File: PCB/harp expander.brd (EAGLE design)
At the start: 124.5 x 80.4 mm, 132 parts, among them IC1 XMEGA-A1TQFP, IC14 SN74LVC1G125DBVT, IC2 USBLC6-2SC6, IC3 FT232RL, IC4 TLV70033DDCR, IC5 TLV70033DDCR, IC6 SI8610BC-B-IS, IC7 SN74LVC1G125DBVT, T10 BC850, T11 BC850, T12 BC850, T13 BC850, T2 BC850, T3 BC850, T4 BC850, T5 BC850, T6 BC850, T7 BC850, T8 BC850, T9 BC850, U1 744245X, U2 744245X

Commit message: Minor corrections.
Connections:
- net IO_BUTTON0 renamed AUX_IN0
- net IO_BUTTON1 renamed AUX_IN1
- net PD0 renamed IO4_UC
- net PD1 renamed IO3_UC
- net PD2 renamed IO2_UC
- net PD3 renamed IO1_UC
- net PD4 renamed IO0_UC
- net PE0 renamed IO5_UC
- net PE1 renamed IO6_UC
- net PE2 renamed IO7_UC
- net PE3 renamed IO8_UC
- net PE4 renamed IO9_UC
- net USER_BUTTON_1 renamed AUX_IN1_UC
- removed net USER_BUTTON_0: IC1.96, IC14.4
- new net AUX_IN0_UC: IC1.37, IC1.96, IC14.4
- new net N$166: IC1.51
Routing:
- net AUX_IN0_UC: track 0.00 -> 31.4 mm, vias 0 -> 2
- net USER_BUTTON_0: track 14.0 -> 0.00 mm
- net STATE: track 98.7 -> 100.2 mm
- removed copper zone on layer 1, net N$83

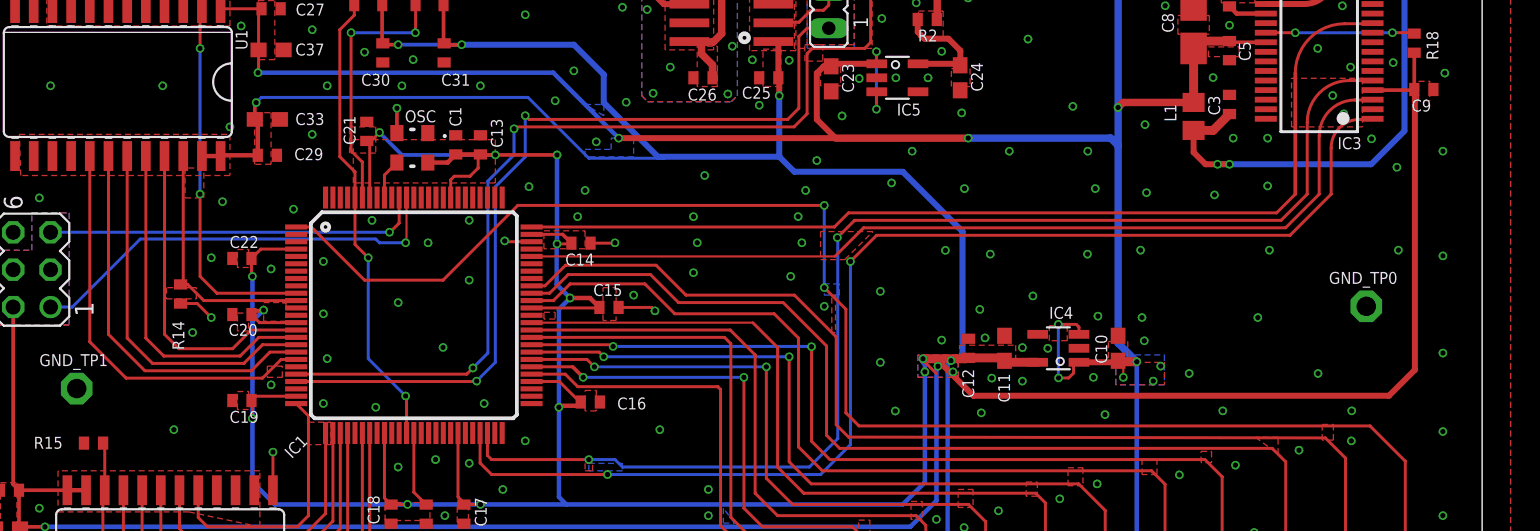
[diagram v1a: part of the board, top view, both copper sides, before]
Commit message: Added ability to connect to a Teensy/Arduino and to read rotary encoders.
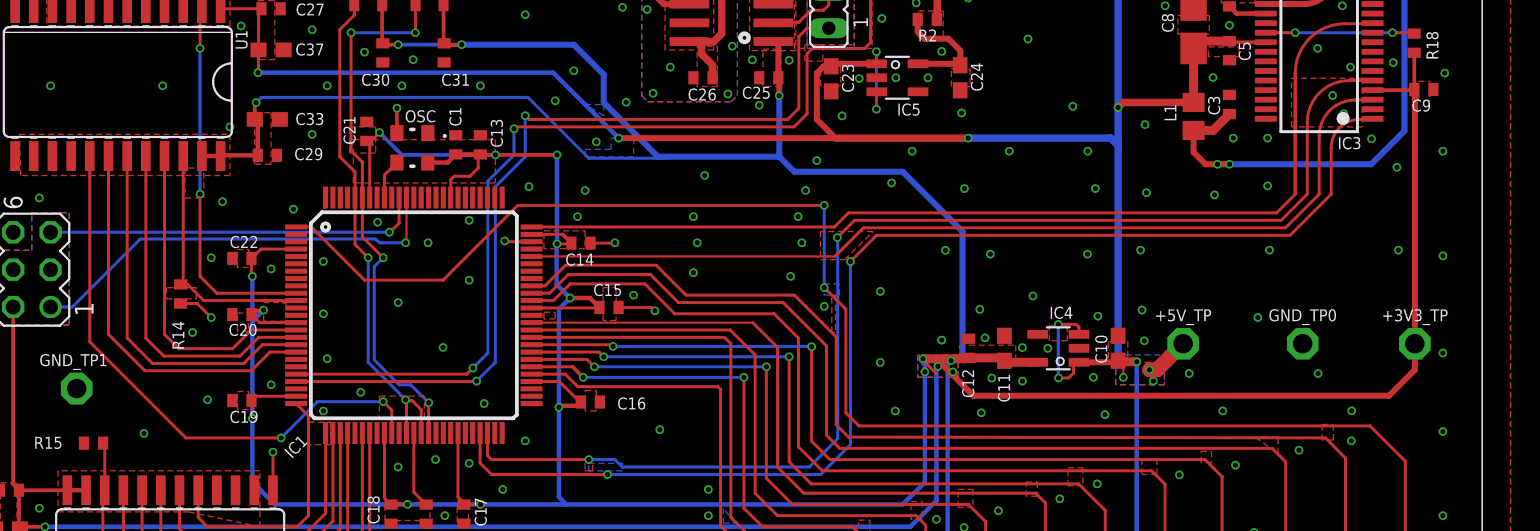
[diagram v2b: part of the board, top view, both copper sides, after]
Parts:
- added +3V3_TP, +5V_TP: TPPAD1-13, testpad:P1-13
- moved GND_TP0 5.01 mm to (112.3, 38.6)
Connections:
- removed net N$166: IC1.51
- net +3V3: now also +3V3_TP.TP
- net +5V: now also +5V_TP.TP
- net AUX_IN0_UC: now also IC1.39
- net AUX_IN1_UC: now also IC1.40
- net IO9_UC: now also IC1.35; no longer IC1.19
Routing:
- net AUX_IN1_UC: track 17.8 -> 36.7 mm, vias 2 -> 4
- net IO9_UC: track 28.2 -> 38.7 mm, vias 0 -> 2
- net +5V: track 287.7 -> 291.2 mm
- net AUX_IN0_UC: track 31.4 -> 34.3 mm
- net GND: vias 303 -> 304

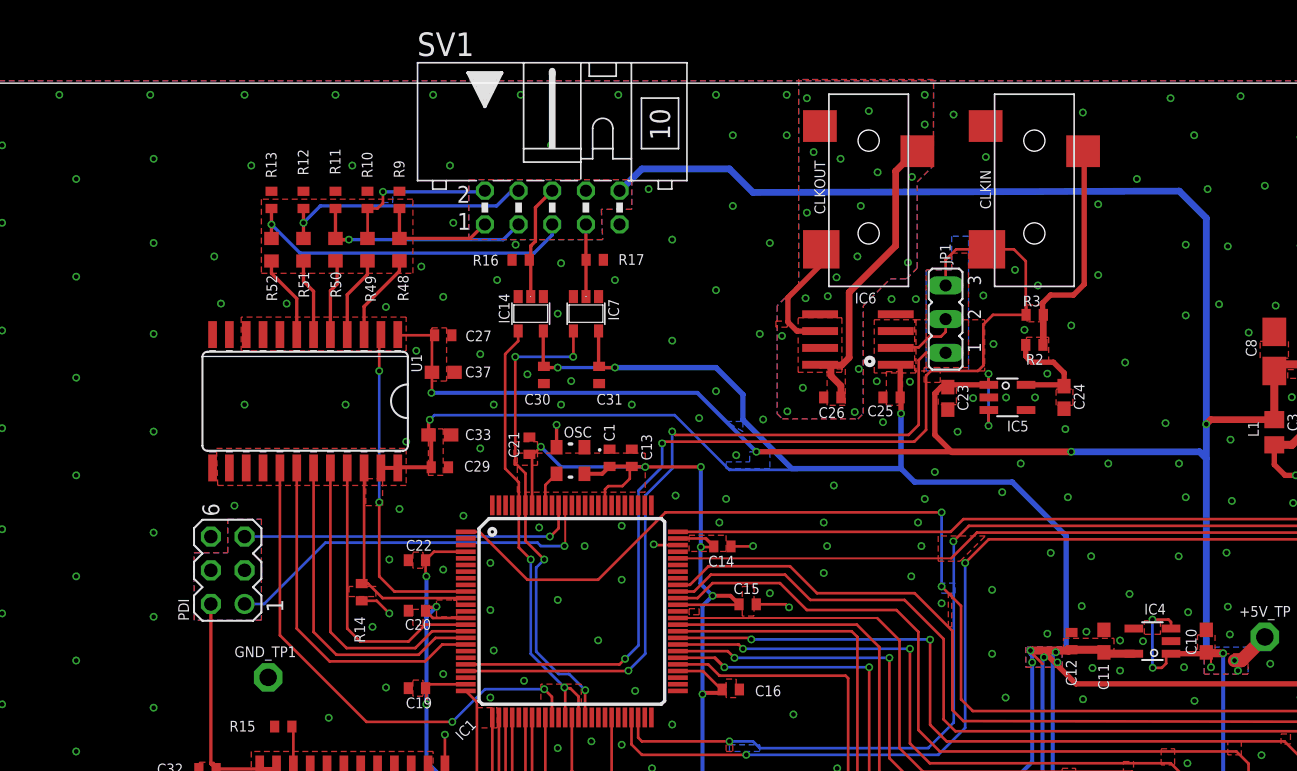
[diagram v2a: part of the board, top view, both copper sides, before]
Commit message: Added ability to be used as a clock generator.
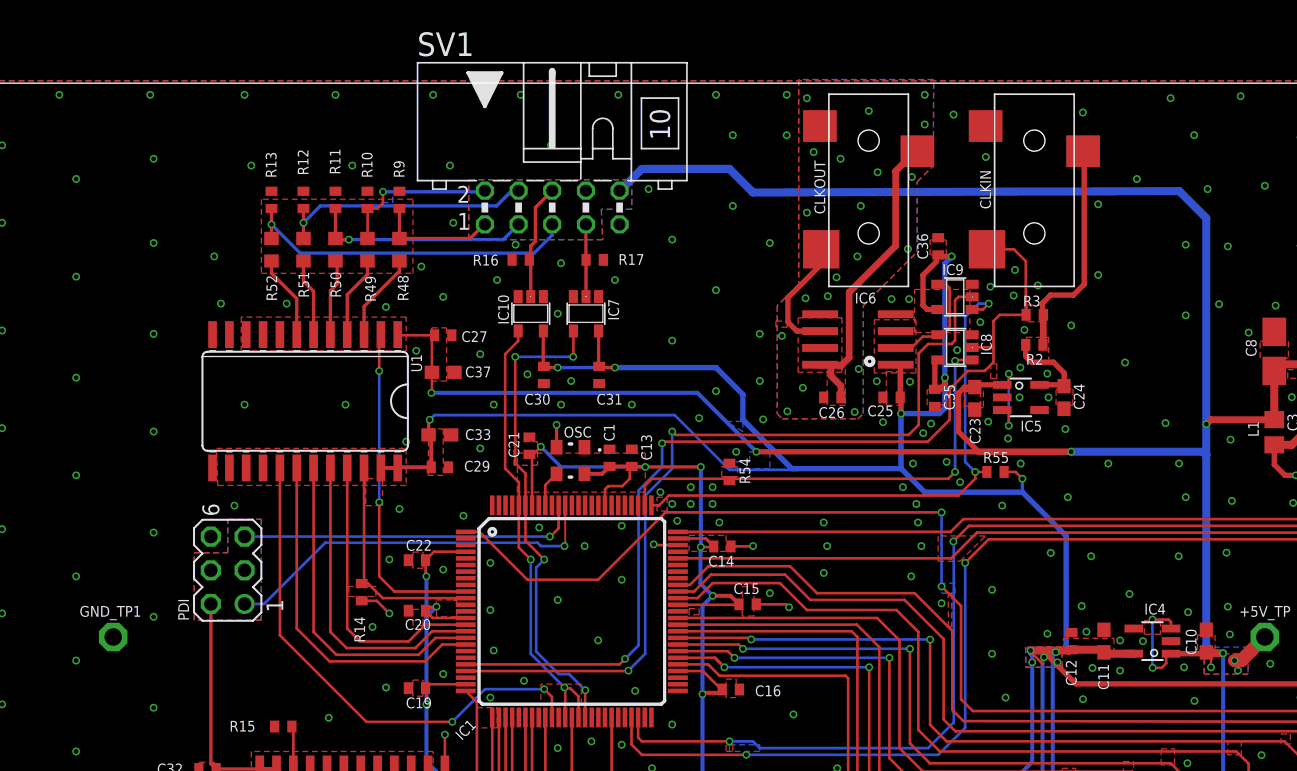
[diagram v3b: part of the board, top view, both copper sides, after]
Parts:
- removed JP1: CLCK Jumper, jumper:JP2
- added C35, C36: 100nF, rcl:C0402
- added IC8, IC9: SN74LVC1G125DBVT, 74xx-little-de:SOT23-5
- added R54, R55: 10k, rcl:R0402
- R53: value 1k -> 10
- moved GND_TP1 12.1 mm to (17.3, 38.6)
- moved C23 2.03 mm to (82.3, 56.6)
- moved IC5 1.02 mm to (85.7, 56.7)
- renumbered IC14 to IC10
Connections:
- new net EN_CLOCK_IN: IC1.77, IC8.1, R54.1
- new net EN_CLOCK_OUT: IC1.76, IC9.1, R55.1
- net +3V3: now also C35.1, C36.1, IC8.5, IC9.5, R55.2
- net CLOCK_IN: now also IC8.2; no longer JP1.3
- net CLOCK_OUT: now also IC9.2; no longer JP1.1
- net GND: now also C35.2, C36.2, IC8.3, IC9.3, R54.2
- net N$43: now also IC8.4, IC9.4; no longer JP1.2
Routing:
- net EN_CLOCK_OUT: track 0.00 -> 42.3 mm, vias 0 -> 2
- net EN_CLOCK_IN: track 0.00 -> 35.2 mm, vias 0 -> 2
- net +3V3: track 526.9 -> 555.0 mm, vias 22 -> 25
- net CLOCK_OUT: track 57.8 -> 63.7 mm
- net CLOCK_IN: track 78.0 -> 73.2 mm
- net N$43: track 5.23 -> 8.85 mm
- net N$42: track 8.17 -> 7.16 mm
- net GND: vias 304 -> 317
- removed copper zone on layer 1, net N$140
- removed copper zone on layer 1, net N$173
- removed copper zone on layer 16, net N$174

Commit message: Minor corrections on layout and schematics.
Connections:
- net AUX_IN0_UC: no longer IC1.96
- net AUX_IN1_UC: no longer IC1.95
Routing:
- net STATE: track 100.2 -> 101.9 mm
- net PDI_CLK: track 25.7 -> 26.5 mm
- net AUX_IN1_UC: track 36.7 -> 36.2 mm
- net GND: vias 317 -> 318

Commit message: Added filtering on inputs and reset lines to prevent erroneous behavior in noisy environments.
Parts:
- removed C8: 4.7uF, rcl:A/3216-18W
- removed R1: 1M, rcl:R0402
- removed R18: 10k, rcl:R0402
- added C39: 100u 25V, rcl:TT2D6
- added C40: 100nF, rcl:C0402
- added C41, C42, C43, C44, C45, C46, C47, C48, C49, C50, C51: 330pF, rcl:C0402
- added C52: 4.7uF, rcl:C0603
- added R56, R57, R58, R59, R60, R61, R62, R63, R64, R65, R66, R67, R68: 10k, rcl:R0402
- added R69: 100R, rcl:R0603
- added U3: 74HCT125SO14, harp input expander:SO14
- CLKIN, CLKOUT: device CNP-connectors:35RASMT2BHNTRX -> harp input expander:35RASMT2BHNTRX
- IC2: device CNP 2:SOT23-6L -> harp input expander:SOT23-6L
- IC5: device CNP:TSOT23-5 -> harp input expander:TSOT23-5
- IC6: device CNP-ics 2:SO-08 -> harp input expander:SO-08
- LED0, LED1, LED2, LED3, LED4, LED5: value 569-0112-100 -> RED_LEDs; device jonnew:569-011X-X00_LED_ARRAY -> harp input expander:569-011X-X00_LED_ARRAY
- OSC: device CNP-miscellaneous:OSCILLATOR_3.2X2.5 -> harp input expander:OSCILLATOR_3.2X2.5
- R53: value 10 -> 10k
- USB: device CNP-connectors:240-0002-1 -> harp input expander:240-0002-1
- moved +3V3_TP 34.4 mm to (85.5, 40.0)
- moved +5V_TP 22.1 mm to (97.2, 59.6)
- moved PDI 17.9 mm to (41.6, 52.3)
- moved R13 11.0 mm to (18.6, 74.6)
- moved R52 10.9 mm to (18.6, 70.5)
- moved L1 10.4 mm to (104.4, 64.4), turned to 90 degrees
- moved C3 9.93 mm to (108.0, 64.8), turned to 270 degrees
- moved GND_TP1 9.12 mm to (8.27, 37.1)
- moved R12 8.95 mm to (23.2, 74.6)
- moved R51 8.82 mm to (23.2, 70.5)
- moved R14 8.09 mm to (30.5, 47.9), turned to 180 degrees
- moved R38 7.92 mm to (23.6, 10.9), turned to 0 degrees
- moved R5 7.92 mm to (23.6, 13.7), turned to 180 degrees
- moved R15 6.41 mm to (23.7, 32.2)
- moved C27 6.31 mm to (35.9, 61.8)
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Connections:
- removed net N$175: IC3.19, R18.2
- new net N$140: R61.1, U1.16
- new net N$143: R60.1, U1.15
- new net N$145: R59.1, U1.14
- new net N$146: R56.1, U1.10
- new net N$165: R57.1, U1.9
- new net N$166: R58.1, U1.8
- new net N$167: R62.1, U2.10
- new net N$169: R63.1, U2.9
- new net N$170: R64.1, U2.8
- new net N$171: R67.1, U2.16
- new net N$172: R66.1, U2.15
- new net N$173: R65.1, U2.14
- new net U_BNC_IOS_DIR: IC1.32, U3.2
- new net U_BNC_IOS_ENBL: IC1.31, U3.5
- new net U_IDE_IOS_DIR: IC1.10, U3.9
- new net U_IDE_IOS_ENBL: IC1.11, U3.12
- net +3V3: now also IC1.51, R68.2; no longer R18.1
- net +5V: now also C39.+, C40.1, C52.1, U3.14; no longer C8.+
- net BNC_IOS_DIR: now also U3.3; no longer IC1.32
- net BNC_IOS_ENBL: now also U3.6; no longer IC1.31
- net GND: now also C39.-, C40.2, C41.2, C42.2, C43.2, C44.2, C45.2, C46.2, C47.2, C48.2, C49.2, C50.2, C51.2, C52.2, R56.2, R57.2, R58.2, R59.2, R60.2, R61.2, R62.2, R63.2, R64.2, R65.2, R66.2, R67.2, R69.2, U3.1, U3.10, U3.13, U3.4, U3.7; no longer C8.-, R1.2
- net IDE_IOS_DIR: now also U3.8; no longer IC1.10
- net IDE_IOS_ENBL: now also U3.11; no longer IC1.11
- net N$114: now also C46.1
- net N$115: now also C45.1
- net N$116: now also C44.1
- net N$122: now also C43.1
- net N$142: now also C42.1
- net N$152: now also C41.1
- net N$6: now also C50.1
- net N$61: now also R69.1; no longer R1.1
- net N$68: now also C49.1
- net N$69: now also C48.1
- net N$97: now also C47.1
- net PDI_CLK: now also C51.1, R68.1
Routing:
- net +5V: track 291.4 -> 334.6 mm, vias 13 -> 14
- net U_BNC_IOS_DIR: track 0.00 -> 29.0 mm, vias 0 -> 2
- net +3V3: track 555.0 -> 581.3 mm
- net U_BNC_IOS_ENBL: track 0.00 -> 25.2 mm, vias 0 -> 2
- net 5VUSB: track 50.6 -> 27.8 mm, vias 4 -> 3
- net BNC_IOS_ENBL: track 34.4 -> 13.4 mm
- net U_IDE_IOS_ENBL: track 0.00 -> 18.9 mm
- net U_IDE_IOS_DIR: track 0.00 -> 18.0 mm
- net PDI_DATA: track 28.9 -> 12.2 mm, vias 1 -> 0
- net IO9: track 25.7 -> 37.6 mm
- net IO8: track 19.5 -> 29.8 mm
- net N$166: track 0.00 -> 10.2 mm
- net N$175: track 10.1 -> 0.00 mm, vias 2 -> 0
- net N$165: track 0.00 -> 9.83 mm
- net BNC_IOS_DIR: track 30.7 -> 21.2 mm, vias 0 -> 2
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- added copper zone on layer 1, net N$150
- added copper zone on layer 16, net N$168
- added copper zone on layer 1, net N$174
- added copper zone on layer 1, net N$175
- added copper zone on layer 1, net N$176
- added copper zone on layer 1, net N$177
- added copper zone on layer 1, net N$178
- added copper zone on layer 1, net N$179
- added copper zone on layer 1, net N$180
- added copper zone on layer 1, net N$193
- added copper zone on layer 1, net N$194
- added copper zone on layer 16, net N$195
- added copper zone on layer 1, net N$196
- added copper zone on layer 1, net N$197
- added copper zone on layer 1, net N$198
- added copper zone on layer 1, net N$199
- added copper zone on layer 1, net N$200
- added copper zone on layer 1, net N$201
- added copper zone on layer 16, net N$202
- added copper zone on layer 1, net N$203
- added copper zone on layer 1, net N$204
- added copper zone on layer 1, net N$205
- added copper zone on layer 16, net N$206
- added copper zone on layer 1, net N$207
- added copper zone on layer 16, net N$208
- added copper zone on layer 16, net N$209
- added copper zone on layer 1, net N$210
- added copper zone on layer 16, net N$211
- added copper zone on layer 1, net N$212
- added copper zone on layer 16, net N$213
- added copper zone on layer 1, net N$214
- added copper zone on layer 16, net N$215
- added copper zone on layer 1, net N$216
- added copper zone on layer 16, net N$217
- added copper zone on layer 16, net N$218
- added copper zone on layer 1, net N$219
- added copper zone on layer 1, net N$220
- added copper zone on layer 1, net N$221
- added copper zone on layer 1, net N$222
- added copper zone on layer 1, net N$223
- added copper zone on layer 1, net N$224
- added copper zone on layer 1, net N$225
- added copper zone on layer 1, net N$226
- added copper zone on layer 1, net N$227
- added copper zone on layer 1, net N$228
- added copper zone on layer 1, net N$229
- added copper zone on layer 16, net N$230
- added copper zone on layer 16, net N$231
- added copper zone on layer 1, net N$232
- added copper zone on layer 1, net N$80
- added copper zone on layer 1, net N$81
- added copper zone on layer 1, net N$82
- added copper zone on layer 1, net N$83
- removed copper zone on layer 1, net N$143
- removed copper zone on layer 16, net N$145
- removed copper zone on layer 1, net N$146
- removed copper zone on layer 1, net N$168
- removed copper zone on layer 1, net N$171
- removed copper zone on layer 16, net N$80
- removed copper zone on layer 16, net N$81
- removed copper zone on layer 16, net N$82
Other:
- board text added: "harp expander v1.2"
- board text removed: "harp expander v1.0"
